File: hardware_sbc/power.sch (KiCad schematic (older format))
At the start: 61 parts, among them J6 Conn_01x02, J7 S2B-PH-K-S(LF)(SN), J8 Conn_01x01_Male, J9 0874380343, U10 MIC94164, U11 BQ29702, U12 BQ27426, U14 CSD85302L, U5 MP2636GR-P, U6 NCP133AMX150TCG

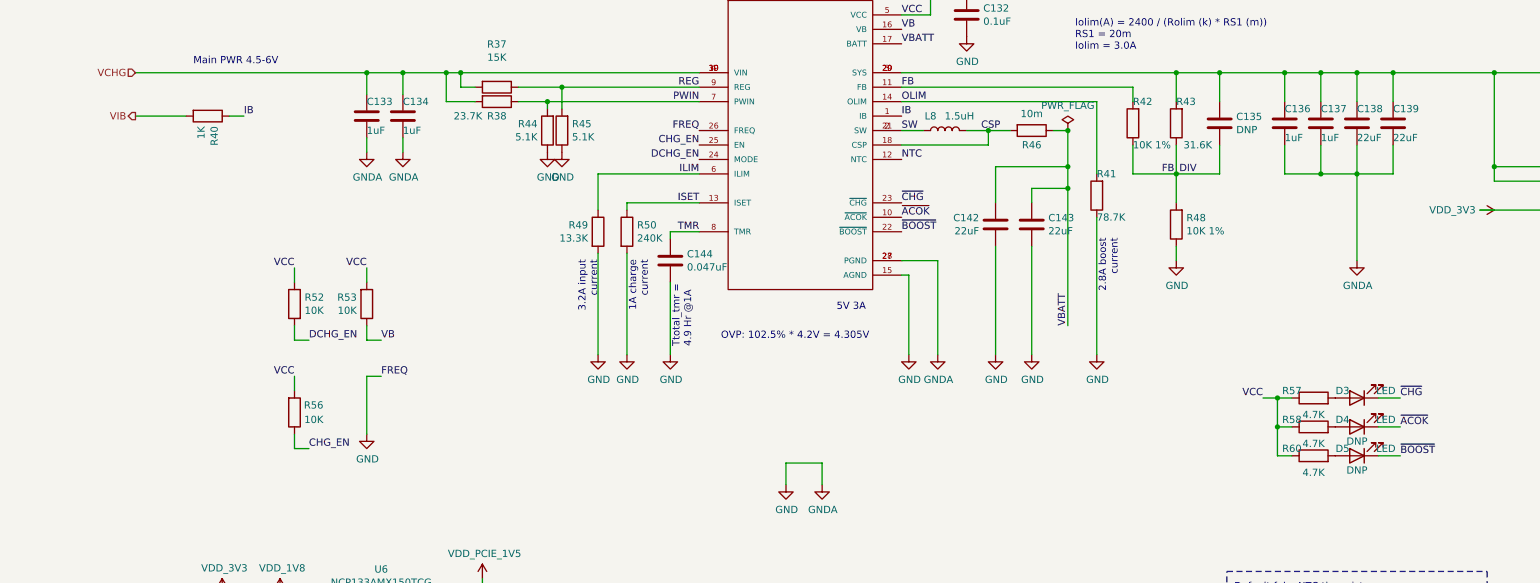
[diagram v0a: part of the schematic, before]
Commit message: Replace system and charger LEDs with smaller 0404 RGB LED
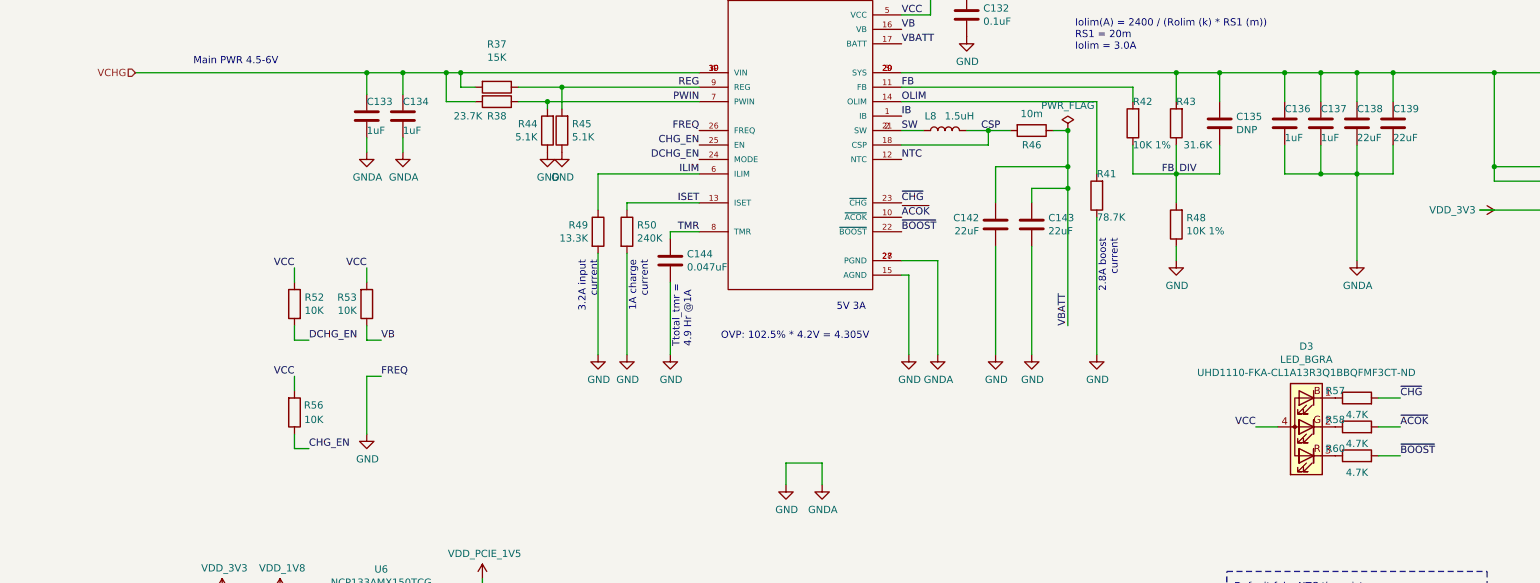
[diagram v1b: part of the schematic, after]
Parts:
- removed D3, D4, D5: LED, LED_SMD:LED_0603_1608Metric, symbol Device:LED
- removed R40: 1K, Resistor_SMD:R_0402_1005Metric, symbol Device:R
- added D3: LED_BGRA, mxenc:LED_0404, symbol Device:LED_BGRA
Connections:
- net VCC: now also D3.4 (A); no longer R57.1, R58.1, R60.1
- net ~ACOK: now also R58.2
- net ~BOOST: now also R60.2
- net ~CHG: now also R57.2
- new net: D3.1 (BK), R57.1
- new net: D3.2 (GK), R58.1
- new net: D3.3 (RK), R60.1
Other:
- moved on the sheet: R57, R58, R60
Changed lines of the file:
@@
 	1    0    0    1
-$EndComp
-Wire Wire Line
-	2300 2700 1950 2700
-Text HLabel 1950 2700 0    50   Output ~ 0
-VIB
-Wire Wire Line
-	2700 2700 2600 2700
-Text Label 2700 2700 0    50   ~ 0
-IB
-$Comp
-L Device:R R40
-U 1 1 5DC8CB6A
-P 2450 2700
-F 0 "R40" H 2520 2746 50  0000 L CNN
-F 1 "1K" H 2520 2655 50  0000 L CNN
-F 2 "Resistor_SMD:R_0402_1005Metric" V 2380 2700 50  0001 C CNN
-F 3 "~" H 2450 2700 50  0001 C CNN
-F 4 "Yageo" H 2450 2700 50  0001 C CNN "Mfgr"
-F 5 "" H 2450 2700 50  0001 C CNN "Part"
-F 6 "311-1.0KJRCT-ND" H 2450 2700 50  0001 C CNN "Vendorpart"
-F 7 "RC0402JR-071KL" H 2450 2700 50  0001 C CNN "Mfgrpart"
-	1    2450 2700
-	0    1    1    0
 $EndComp
 $Comp
@@
 L Device:R R?
 U 1 1 5F3EE159
-P 10100 4650
+P 10400 4650
 AR Path="/5F3EE159" Ref="R?"  Part="1"
 AR Path="/5DC6F4F1/5F3EE159" Ref="R57"  Part="1"
-F 0 "R57" V 10150 4800 50  0000 C CNN
-F 1 "4.7K" V 9984 4650 50  0000 C CNN
-F 2 "Resistor_SMD:R_0201_0603Metric" V 10030 4650 50  0001 C CNN
-F 3 "~" H 10100 4650 50  0001 C CNN
-F 4 "Yageo" H 10100 4650 50  0001 C CNN "Mfgr"
-F 5 "" H 10100 4650 50  0001 C CNN "Part"
-F 6 "311-4.7KNCT-ND" H 10100 4650 50  0001 C CNN "Vendorpart"
-F 7 "RC0201JR-074K7L" H 10100 4650 50  0001 C CNN "Mfgrpart"
-	1    10100 4650
+F 0 "R57" V 10450 4800 50  0000 C CNN
+F 1 "4.7K" V 10284 4650 50  0000 C CNN
+F 2 "Resistor_SMD:R_0201_0603Metric" V 10330 4650 50  0001 C CNN
+F 3 "~" H 10400 4650 50  0001 C CNN
+F 4 "Yageo" H 10400 4650 50  0001 C CNN "Mfgr"
+F 5 "" H 10400 4650 50  0001 C CNN "Part"
+F 6 "311-4.7KNCT-ND" H 10400 4650 50  0001 C CNN "Vendorpart"
+F 7 "RC0201JR-074K7L" H 10400 4650 50  0001 C CNN "Mfgrpart"
+	1    10400 4650
 	0    -1   -1   0
 $EndComp
@@
 L Device:R R?
 U 1 1 5F4012DC
-P 10100 4850
+P 10400 4850
 AR Path="/5F4012DC" Ref="R?"  Part="1"
 AR Path="/5DC6F4F1/5F4012DC" Ref="R58"  Part="1"
-F 0 "R58" V 10150 5000 50  0000 C CNN
-F 1 "4.7K" V 9984 4850 50  0000 C CNN
-F 2 "Resistor_SMD:R_0201_0603Metric" V 10030 4850 50  0001 C CNN
-F 3 "~" H 10100 4850 50  0001 C CNN
-F 4 "Yageo" H 10100 4850 50  0001 C CNN "Mfgr"
-F 5 "" H 10100 4850 50  0001 C CNN "Part"
-F 6 "311-4.7KNCT-ND" H 10100 4850 50  0001 C CNN "Vendorpart"
-F 7 "RC0201JR-074K7L" H 10100 4850 50  0001 C CNN "Mfgrpart"
-	1    10100 4850
+F 0 "R58" V 10450 5000 50  0000 C CNN
+F 1 "4.7K" V 10284 4850 50  0000 C CNN
+F 2 "Resistor_SMD:R_0201_0603Metric" V 10330 4850 50  0001 C CNN
+F 3 "~" H 10400 4850 50  0001 C CNN
+F 4 "Yageo" H 10400 4850 50  0001 C CNN "Mfgr"
+F 5 "" H 10400 4850 50  0001 C CNN "Part"
+F 6 "311-4.7KNCT-ND" H 10400 4850 50  0001 C CNN "Vendorpart"
+F 7 "RC0201JR-074K7L" H 10400 4850 50  0001 C CNN "Mfgrpart"
+	1    10400 4850
 	0    -1   -1   0
 $EndComp
@@
 L Device:R R?
 U 1 1 5F401539
-P 10100 5050
+P 10400 5050
 AR Path="/5F401539" Ref="R?"  Part="1"
 AR Path="/5DC6F4F1/5F401539" Ref="R60"  Part="1"
-F 0 "R60" V 10150 5200 50  0000 C CNN
-F 1 "4.7K" V 9984 5050 50  0000 C CNN
-F 2 "Resistor_SMD:R_0201_0603Metric" V 10030 5050 50  0001 C CNN
-F 3 "~" H 10100 5050 50  0001 C CNN
-F 4 "Yageo" H 10100 5050 50  0001 C CNN "Mfgr"
-F 5 "" H 10100 5050 50  0001 C CNN "Part"
-F 6 "311-4.7KNCT-ND" H 10100 5050 50  0001 C CNN "Vendorpart"
-F 7 "RC0201JR-074K7L" H 10100 5050 50  0001 C CNN "Mfgrpart"
-	1    10100 5050
+F 0 "R60" V 10450 5200 50  0000 C CNN
+F 1 "4.7K" V 10284 5050 50  0000 C CNN
+F 2 "Resistor_SMD:R_0201_0603Metric" V 10330 5050 50  0001 C CNN
+F 3 "~" H 10400 5050 50  0001 C CNN
+F 4 "Yageo" H 10400 5050 50  0001 C CNN "Mfgr"
+F 5 "" H 10400 5050 50  0001 C CNN "Part"
+F 6 "311-4.7KNCT-ND" H 10400 5050 50  0001 C CNN "Vendorpart"
+F 7 "RC0201JR-074K7L" H 10400 5050 50  0001 C CNN "Mfgrpart"
+	1    10400 5050
 	0    -1   -1   0
 $EndComp
-Text Label 9750 4650 2    50   ~ 0
+Text Label 9700 4850 2    50   ~ 0
 VCC
-Wire Wire Line
-	9750 4650 9850 4650
-Wire Wire Line
-	9850 4650 9850 4850
-Wire Wire Line
-	9850 4850 9950 4850
-Connection ~ 9850 4650
-Wire Wire Line
-	9850 4650 9950 4650
-Wire Wire Line
-	9850 4850 9850 5050
-Wire Wire Line
-	9850 5050 9950 5050
-Connection ~ 9850 4850
-$Comp
-L Device:LED D4
-U 1 1 5F439666
-P 10400 4850
-F 0 "D4" H 10500 4800 50  0000 C CNN
-F 1 "LED" H 10200 4800 50  0000 C CNN
-F 2 "LED_SMD:LED_0603_1608Metric" H 10400 4850 50  0001 C CNN
-F 3 "~" H 10400 4850 50  0001 C CNN
-F 4 "732-4971-1-ND" H 10393 4686 50  0001 C CNN "Vendorpart"
-F 5 "Wurth" H 10400 4850 50  0001 C CNN "Mfgr"
-F 6 "DNP" H 10400 4950 50  0000 C CNN "Populate"
-F 7 "" H 10400 4850 50  0001 C CNN "Part"
-F 8 "150060GS75000" H 10400 4850 50  0001 C CNN "Mfgrpart"
-	1    10400 4850
-	-1   0    0    1
-$EndComp
-$Comp
-L Device:LED D5
-U 1 1 5F439B5B
-P 10400 5050
-F 0 "D5" H 10500 5000 50  0000 C CNN
-F 1 "LED" H 10200 5000 50  0000 C CNN
-F 2 "LED_SMD:LED_0603_1608Metric" H 10400 5050 50  0001 C CNN
-F 3 "~" H 10400 5050 50  0001 C CNN
-F 4 "732-4971-1-ND" H 10393 4795 50  0001 C CNN "Vendorpart"
-F 5 "Wurth" H 10400 5050 50  0001 C CNN "Mfgr"
-F 6 "DNP" H 10400 5150 50  0000 C CNN "Populate"
-F 7 "" H 10400 5050 50  0001 C CNN "Part"
-F 8 "150060GS75000" H 10400 5050 50  0001 C CNN "Mfgrpart"
-	1    10400 5050
-	-1   0    0    1
-$EndComp
 Text Label 12250 7200 3    50   ~ 0
 VBATT
@@
 Wire Wire Line
 	7700 2800 7850 2800
-$Comp
-L Device:LED D3
-U 1 1 5F37B40E
-P 10400 4650
-F 0 "D3" H 10500 4600 50  0000 C CNN
-F 1 "LED" H 10200 4600 50  0000 C CNN
-F 2 "LED_SMD:LED_0603_1608Metric" H 10400 4650 50  0001 C CNN
-F 3 "~" H 10400 4650 50  0001 C CNN
-F 4 "732-4971-1-ND" H 10393 4486 50  0001 C CNN "Vendorpart"
-F 5 "Wurth" H 10400 4650 50  0001 C CNN "Mfgr"
-F 6 "" H 10400 4650 50  0001 C CNN "Part"
-F 7 "150060GS75000" H 10400 4650 50  0001 C CNN "Mfgrpart"
-	1    10400 4650
-	-1   0    0    1
-$EndComp
 Connection ~ 13950 3050
 Wire Wire Line
@@
 Wire Wire Line
 	3050 4500 3050 4600
+$Comp
+L Device:LED_BGRA D3
+U 1 1 60335234
+P 10050 4850
+F 0 "D3" H 10050 4293 50  0000 C CNN
+F 1 "LED_BGRA" H 10050 4384 50  0000 C CNN
+F 2 "mxenc:LED_0404" H 10050 4800 50  0001 C CNN
+F 3 "~" H 10050 4800 50  0001 C CNN
+F 4 "UHD1110-FKA-CL1A13R3Q1BBQFMF3CT-ND " H 10050 4475 50  0000 C CNN "Vendorpart"
+F 5 "Cree" H 10050 4850 50  0001 C CNN "Mfgr"
+F 6 "UHD1110-FKA" H 10050 4850 50  0001 C CNN "Mfgrpart"
+	1    10050 4850
+	-1   0    0    1
+$EndComp
+Wire Wire Line
+	9700 4850 9850 4850
 $EndSCHEMATC

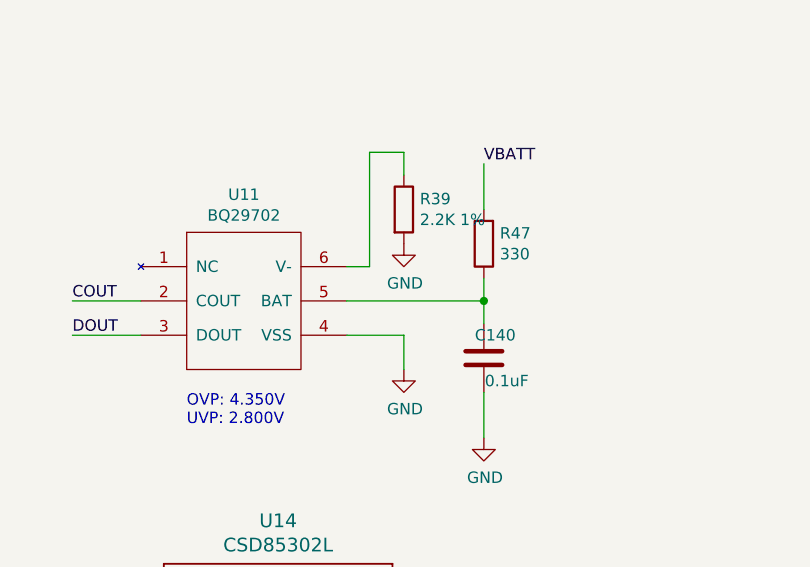
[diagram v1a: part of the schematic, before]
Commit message: Add vbus to expansion connector and bugfix for battery cutoff
This will allow lids to supply power to charge the battery.

The battery cutoff circuit needs V- connected to pack ground, so
this was also fixed.
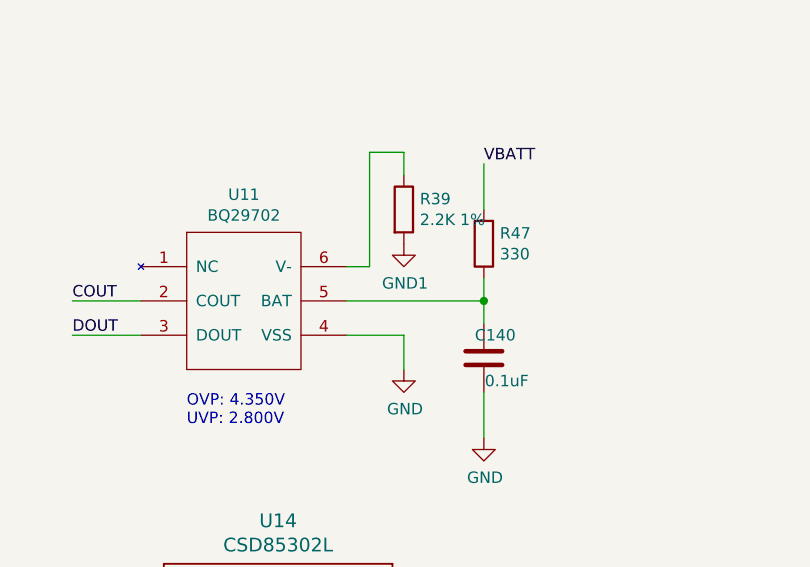
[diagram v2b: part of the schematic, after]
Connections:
- net GND: no longer R39.2
- net GND1: now also R39.2
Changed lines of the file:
@@
 	7250 6850 7350 6850
-$Comp
-L power:GND #PWR0230
-U 1 1 5EAF1C2F
-P 7500 6750
-F 0 "#PWR0230" H 7500 6500 50  0001 C CNN
-F 1 "GND" H 7505 6577 50  0000 C CNN
-F 2 "" H 7500 6750 50  0001 C CNN
-F 3 "" H 7500 6750 50  0001 C CNN
-	1    7500 6750
-	1    0    0    -1
-$EndComp
 $Comp
 L Device:R R?
@@
 Wire Wire Line
 	9700 4850 9850 4850
+$Comp
+L power:GND1 #PWR?
+U 1 1 6057737F
+P 7500 6750
+F 0 "#PWR?" H 7500 6500 50  0001 C CNN
+F 1 "GND1" H 7505 6577 50  0000 C CNN
+F 2 "" H 7500 6750 50  0001 C CNN
+F 3 "" H 7500 6750 50  0001 C CNN
+	1    7500 6750
+	1    0    0    -1
+$EndComp
 $EndSCHEMATC

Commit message: Change common 22uF part from 4V to 6.3V
Most placements don't require 5V, but a few do. The 4V part is no
longer stocking as well, and price is similar, so change all to
6.3V version.
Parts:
- C138, C139, C142, C143: Mfgrpart GRM188C80G226MEA0D -> GRM188C80J226ME15D; Vendorpart 490-7196-1-ND -> 490-10471-1-ND
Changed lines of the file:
@@
 F 4 "Murata" H 7900 3450 50  0001 C CNN "Mfgr"
 F 5 "" H 7900 3450 50  0001 C CNN "Part"
-F 6 "490-7196-1-ND" H 7900 3450 50  0001 C CNN "Vendorpart"
-F 7 "GRM188C80G226MEA0D" H 7900 3450 50  0001 C CNN "Mfgrpart"
+F 6 "490-10471-1-ND" H 7900 3450 50  0001 C CNN "Vendorpart"
+F 7 "GRM188C80J226ME15D" H 7900 3450 50  0001 C CNN "Mfgrpart"
 	1    7900 3450
 	-1   0    0    1
@@
 F 4 "Murata" H 8150 3450 50  0001 C CNN "Mfgr"
 F 5 "" H 8150 3450 50  0001 C CNN "Part"
-F 6 "490-7196-1-ND" H 8150 3450 50  0001 C CNN "Vendorpart"
-F 7 "GRM188C80G226MEA0D" H 8150 3450 50  0001 C CNN "Mfgrpart"
+F 6 "490-10471-1-ND" H 8150 3450 50  0001 C CNN "Vendorpart"
+F 7 "GRM188C80J226ME15D" H 8150 3450 50  0001 C CNN "Mfgrpart"
 	1    8150 3450
 	-1   0    0    1
@@
 F 4 "Murata" H 10400 2750 50  0001 C CNN "Mfgr"
 F 5 "" H 10400 2750 50  0001 C CNN "Part"
-F 6 "490-7196-1-ND" H 10400 2750 50  0001 C CNN "Vendorpart"
-F 7 "GRM188C80G226MEA0D" H 10400 2750 50  0001 C CNN "Mfgrpart"
+F 6 "490-10471-1-ND" H 10400 2750 50  0001 C CNN "Vendorpart"
+F 7 "GRM188C80J226ME15D" H 10400 2750 50  0001 C CNN "Mfgrpart"
 	1    10400 2750
 	-1   0    0    1
@@
 F 4 "Murata" H 10650 2750 50  0001 C CNN "Mfgr"
 F 5 "" H 10650 2750 50  0001 C CNN "Part"
-F 6 "490-7196-1-ND" H 10650 2750 50  0001 C CNN "Vendorpart"
-F 7 "GRM188C80G226MEA0D" H 10650 2750 50  0001 C CNN "Mfgrpart"
+F 6 "490-10471-1-ND" H 10650 2750 50  0001 C CNN "Vendorpart"
+F 7 "GRM188C80J226ME15D" H 10650 2750 50  0001 C CNN "Mfgrpart"
 	1    10650 2750
 	-1   0    0    1

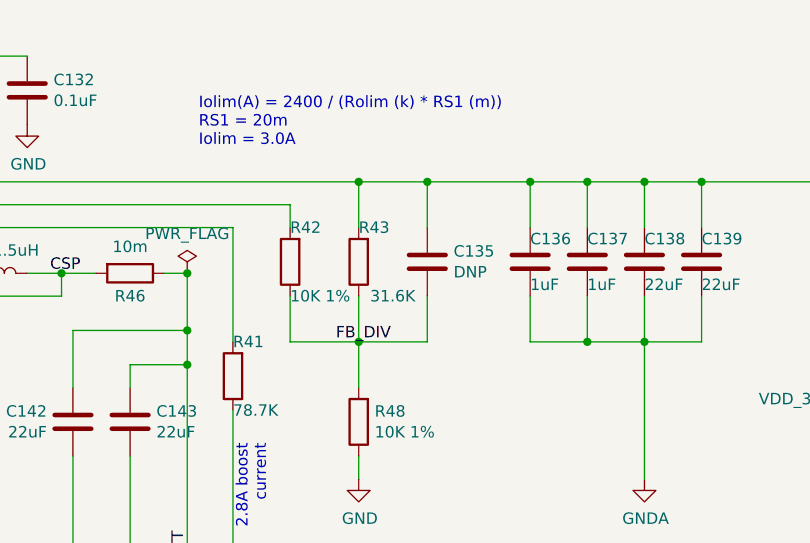
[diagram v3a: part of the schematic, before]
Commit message: Remove boost feedback resistor R42
This part was added in error, take it out
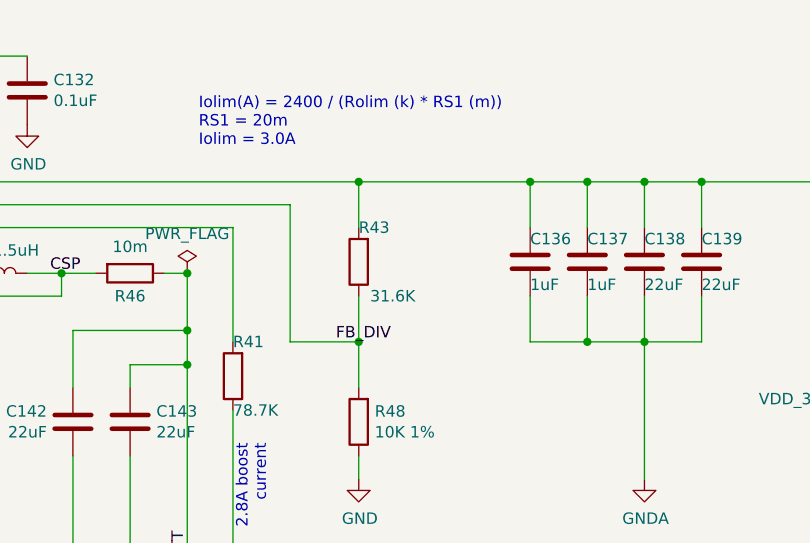
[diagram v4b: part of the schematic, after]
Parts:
- removed C135: DNP, Capacitor_SMD:C_0402_1005Metric, symbol Device:C
- removed R42: 10K 1%, Resistor_SMD:R_0201_0603Metric, symbol Device:R
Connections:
- net FB_DIV is gone; now on net FB: R43.1, R48.2
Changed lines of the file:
@@
 	7250 2800 7400 2800
-Wire Wire Line
-	8850 2600 8850 2500
 Wire Wire Line
 	8850 2500 7250 2500
@@
 	9150 2900 9150 3100
 Wire Wire Line
-	8850 2900 8850 3100
-Wire Wire Line
 	8850 3100 9150 3100
 Connection ~ 9150 3100
@@
 	10400 2400 10650 2400
 Wire Wire Line
-	9150 2400 9450 2400
-Wire Wire Line
 	9900 2400 10150 2400
-$Comp
-L Device:C C135
-U 1 1 5EFB836F
-P 9450 2750
-F 0 "C135" H 9565 2796 50  0000 L CNN
-F 1 "DNP" H 9565 2705 50  0000 L CNN
-F 2 "Capacitor_SMD:C_0402_1005Metric" H 9488 2600 50  0001 C CNN
-F 3 "~" H 9450 2750 50  0001 C CNN
-F 4 "DNP" H 9450 2750 50  0001 C CNN "Populate"
-	1    9450 2750
-	1    0    0    -1
-$EndComp
-Wire Wire Line
-	9150 3100 9450 3100
-Wire Wire Line
-	9450 3100 9450 2900
-Wire Wire Line
-	9450 2600 9450 2400
-Connection ~ 9450 2400
-Wire Wire Line
-	9450 2400 9900 2400
 $Comp
 L Device:C C?
@@
 F 7 "RC0201FR-0778R7L" H 8600 3250 50  0001 C CNN "Mfgrpart"
 	1    8600 3250
-	-1   0    0    1
-$EndComp
-$Comp
-L Device:R R42
-U 1 1 5EF37B7F
-P 8850 2750
-F 0 "R42" H 8850 2600 50  0000 R CNN
-F 1 "10K 1%" H 8850 2900 50  0000 R CNN
-F 2 "Resistor_SMD:R_0201_0603Metric" V 8780 2750 50  0001 C CNN
-F 3 "~" H 8850 2750 50  0001 C CNN
-F 4 "311-10.0KMCT-ND" H 8780 2841 50  0001 R CNN "Vendorpart"
-F 5 "Yageo" H 8850 2750 50  0001 C CNN "Mfgr"
-F 6 "" H 8850 2750 50  0001 C CNN "Part"
-F 7 "RC0201FR-0710KL" H 8850 2750 50  0001 C CNN "Mfgrpart"
-	1    8850 2750
 	-1   0    0    1
 $EndComp
@@
 	9700 4850 9850 4850
 $Comp
-L power:GND1 #PWR?
+L power:GND1 #PWR0158
 U 1 1 6057737F
 P 7500 6750
-F 0 "#PWR?" H 7500 6500 50  0001 C CNN
+F 0 "#PWR0158" H 7500 6500 50  0001 C CNN
 F 1 "GND1" H 7505 6577 50  0000 C CNN
 F 2 "" H 7500 6750 50  0001 C CNN
@@
 	1    0    0    -1
 $EndComp
+Wire Wire Line
+	8850 2500 8850 3100
+Wire Wire Line
+	9150 2400 9900 2400
 $EndSCHEMATC
